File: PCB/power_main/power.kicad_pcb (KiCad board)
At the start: 4 copper layers, 40.9 x 58 mm, 82 parts, among them IC1 TPS7A2450DBVR, IC2 TPD4S480RUKR, IC3 CAT24C512WI-GT3, J2 DX07P024AJ1R1500, J3 Conn_02x10_Counter_Clockwise, J4 Conn_02x10_Counter_Clockwise, J5 DX07S024JJ2R1300, J6 DX07S024JJ2R1300, Q1 CSD18543Q3A, Q2 2N7002DW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

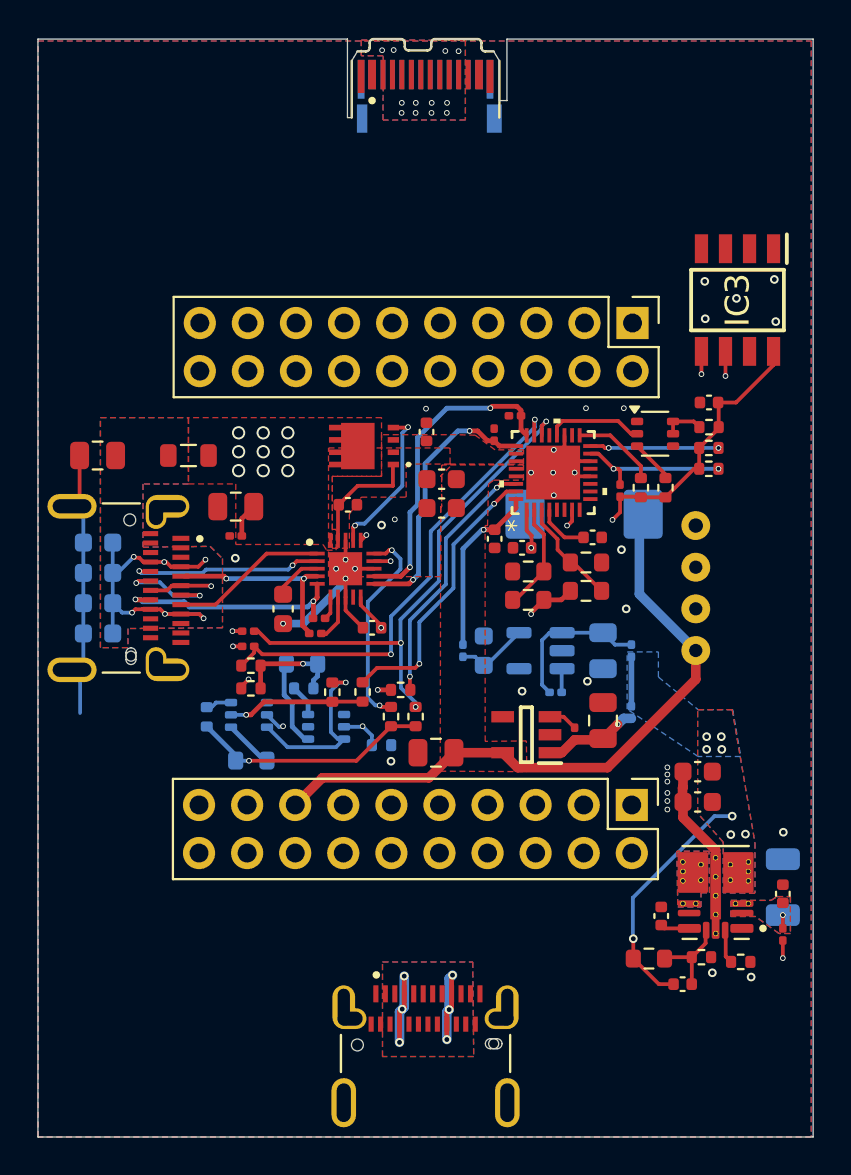
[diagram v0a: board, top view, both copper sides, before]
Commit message: removed POWER_PATH_EN logic add more doku and pictires for context
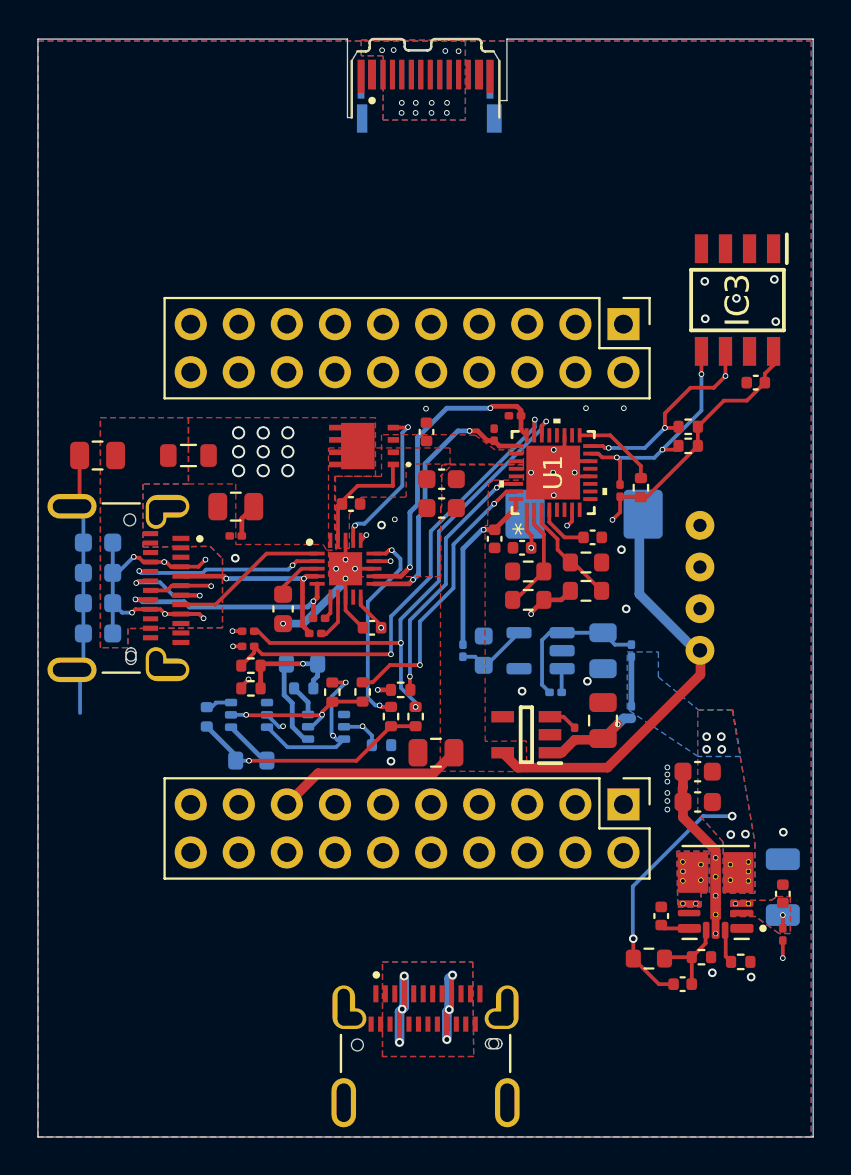
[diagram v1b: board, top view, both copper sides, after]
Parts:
- removed Q2: 2N7002DW, Package_TO_SOT_SMD:SOT-363_SC-70-6
- removed R1, R2: 1.00k, Resistor_SMD:R_0402_1005Metric
- IC1: value TPS7A2450DBVR -> TPS7A24
- IC2: value TPD4S480RUKR -> TPD4S480
- IC3: value CAT24C512WI-GT3 -> CAT24C512
- J2: value DX07P024AJ1R1500 -> DX07P024AJ1R1500 - Plug
- J5, J6: value DX07S024JJ2R1300 -> DX07S024JJ2R1300 - Connector
- PS1: value TPSM365R15RDNR -> TPSM365R6; footprint footprints:CONV_TPSM365R15RDNR -> Library:CONV_TPSM365R15RDNR
- U1: value TPS26750SRSMR -> TPS26750; footprint footprints:VQFN32_RSM_TEX -> Library:VQFN32_RSM_TEX
- U26: value fakeMag4pinFemale -> fakeMag4pinMale; footprint Library:fakemag4pin90degFemale -> Library:fakemag4pin90degMale
- moved C12 2.68 mm to (148.9, 69.2)
- moved R7 1.63 mm to (145.3, 72.5), turned to 180 degrees
- moved R6 1.56 mm to (145.3, 71.5), turned to 180 degrees
- moved J3 0.48 mm to (141.9, 66.1)
- moved J4 0.44 mm to (141.9, 91.4)
- moved U26 0.22 mm to (146.0, 80.0), turned to 0 degrees
- moved C1 0.17 mm to (127.5, 75.6)
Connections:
- net D00 renamed /DO0
- Q9 pad 2: Net-(Q9A-G) -> /GPIO_PF
- R97 pad 2: Net-(Q9A-G) -> /GPIO_PF
- R98 pad 2: Net-(Q9A-G) -> /GPIO_PF
- U1 pad 20: Net-(Q2A-G) -> unconnected-(U1-POWER_PATH_EN-Pad20)
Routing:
- net /GPIO_PF: track 0.00 -> 8.50 mm, vias 0 -> 2
- net Net-(Q9A-G): track 7.34 -> 0.00 mm, vias 1 -> 0
- net Net-(Q2A-G): track 5.10 -> 0.00 mm
- net GND: track 32.2 -> 36.2 mm
- net Net-(Q2B-D): track 2.31 -> 0.00 mm
- net /I2Cc_SDA: track 14.8 -> 12.6 mm
- net Net-(Q2A-D): track 2.16 -> 0.00 mm
- net +5V: track 34.9 -> 32.8 mm
- net /I2Cc_SCL: track 12.1 -> 11.2 mm
- net +3V3: track 53.0 -> 52.3 mm, vias 5 -> 6
